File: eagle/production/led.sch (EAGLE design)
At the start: 12 parts, among them Q1 TIP120, Q2 TIP120, Q3 TIP120, U1 ATMEGA328P_PDIP

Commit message: [Eagle] Edited schema and board
Signed-off-by: Roman3349 <ondracek.roman@centrum.cz>
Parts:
- removed SV2: (no value), con-lstb:MA03-2
- added SV3: (no value), con-lstb:MA05-2
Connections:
- net +5V: now also SV3.2; no longer SV2.2
- net GND: now also SV3.10, SV3.4; no longer SV2.6
- net N$14: now also SV3.7; no longer SV2.3
- net N$2: now also SV3.9; no longer SV2.1
- net N$5: now also SV3.5; no longer SV2.5
- net N$6: now also SV3.1; no longer SV2.4

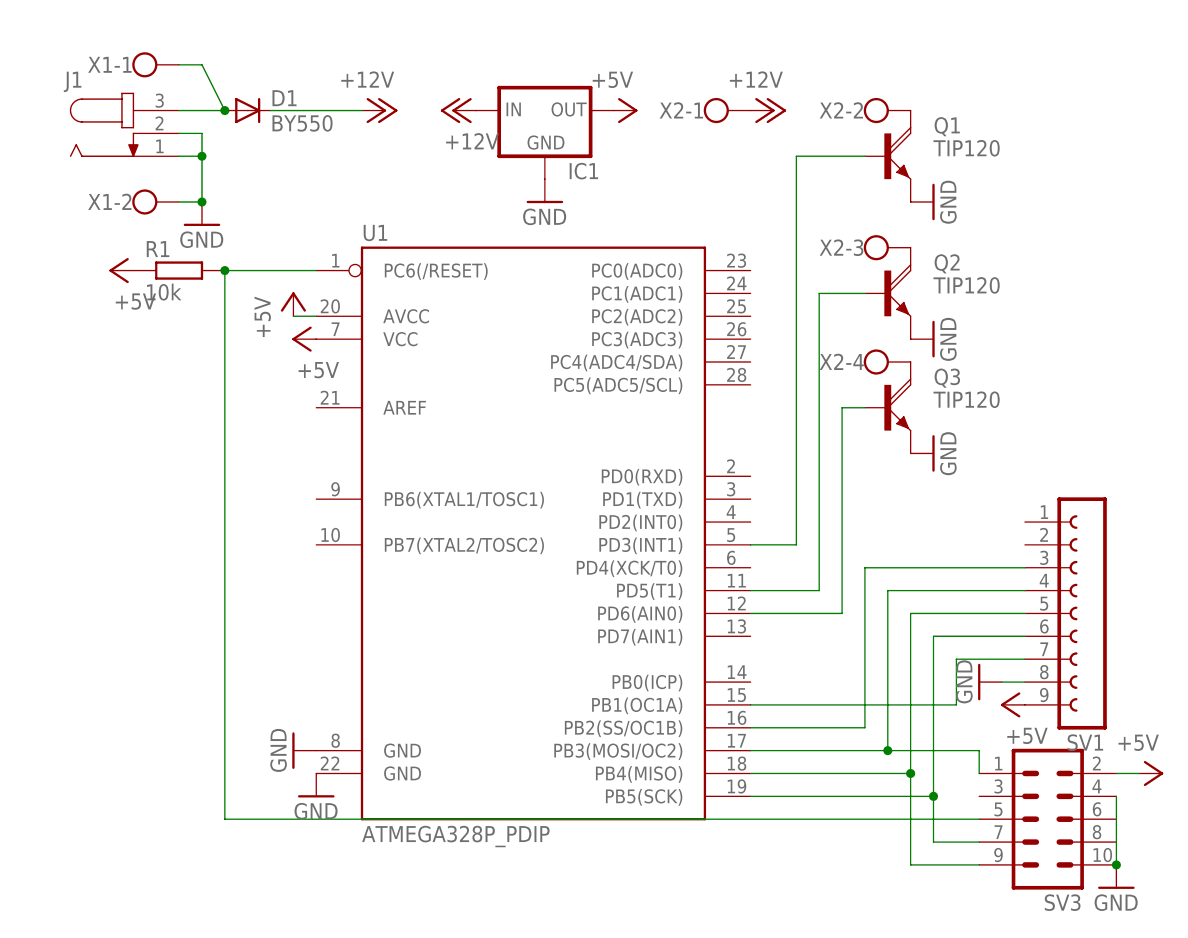
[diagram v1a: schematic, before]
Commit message: [Eagle] Added capacitors and resistors
Signed-off-by: Roman3349 <ondracek.roman@centrum.cz>
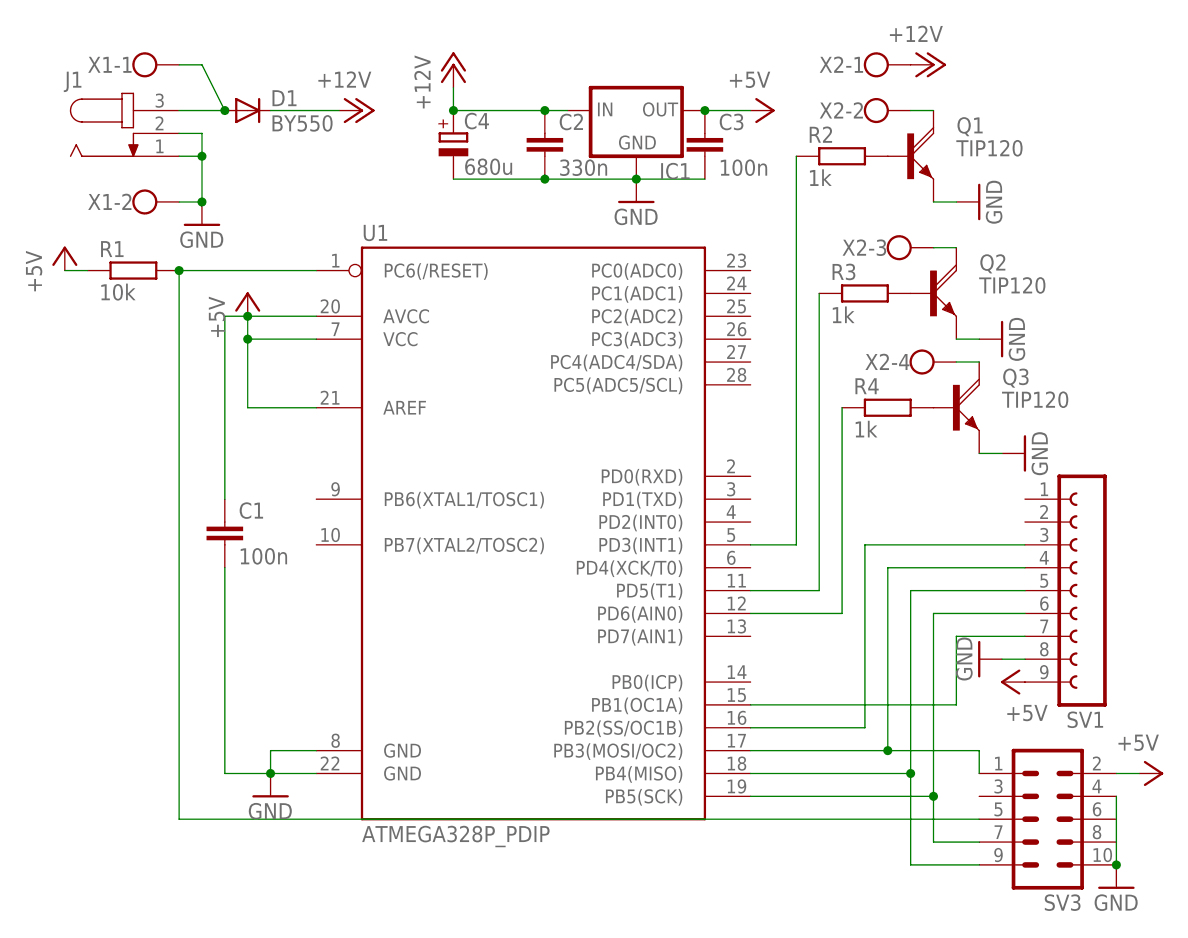
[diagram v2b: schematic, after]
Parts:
- added C1, C3: 100n, rcl:C-EU050-024X044
- added C2: 330n, rcl:C-EU050-024X044
- added C4: 680u, rcl:CPOL-EUE5-10.5
- added R2, R3, R4: 1k, rcl:R-EU_0207/10
- R1: device resistor:R-EU_0207/12 -> resistor:R-EU_0207/10
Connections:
- new net N$15: Q2.B, R3.2
- new net N$16: Q3.B, R4.2
- new net N$4: Q1.B, R2.2
- net +12V: now also C2.1, C4.+
- net +5V: now also C1.1, C3.1, U1.AREF
- net GND: now also C1.2, C2.2, C3.2, C4.-
- net N$11: now also R4.1; no longer Q3.B
- net N$12: now also R3.1; no longer Q2.B
- net N$13: now also R2.1; no longer Q1.B
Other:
- moved on the sheet: IC1, Q1, Q2, Q3, R1, SV1, X2-1, X2-3, X2-4

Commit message: Updated schema and board
Signed-off-by: Roman3349 <ondracek.roman@centrum.cz>
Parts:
- added C5, C6: 18p, rcl:C-EU050-024X044
- added Q4: 16MHz, crystal:CRYSTALHC49S
- C2: value 330n -> 100n
- C4: value 680u -> 470u
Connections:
- new net N$17: C6.1, Q4.2, U1.PB6(XTAL1/TOSC1)
- new net N$18: C5.2, Q4.1, U1.PB7(XTAL2/TOSC2)
- net GND: now also C5.1, C6.2
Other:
- moved on the sheet: C1, U1
